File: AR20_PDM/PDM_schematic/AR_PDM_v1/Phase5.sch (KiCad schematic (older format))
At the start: 10 parts, among them Q3 BTS50025-1TAD, U4 INA233

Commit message: Working on pcb layout
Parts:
- removed D?: D_Schottky_x2, symbol AR20_PDM_v1-rescue:D_Schottky_x2
- added D45, D46: D_Schottky_BAT60A, AR_PDM_v1:D_Shotky_BAT60_HandSoldering, symbol AR20_PDM_v1-rescue:D_Schottky_BAT60A
- gave numbers to parts that had none: 4
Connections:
- net GND: now also D45.2 (A), D46.2 (A)
- net at R28.1, U4.10 (IN+): now also D46.1 (K)
- net at R24.1, U4.9 (In-): now also D45.1 (K)
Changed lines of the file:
@@
 AR Path="/5E0FBBBD/5EE9B23A" Ref="R?"  Part="1"
 AR Path="/5E0FC3A2/5EE9B23A" Ref="R?"  Part="1"
-AR Path="/5E0FCFDC/5EE9B23A" Ref="R?"  Part="1"
+AR Path="/5E0FCFDC/5EE9B23A" Ref="R25"  Part="1"
 AR Path="/5E0FDCCC/5EE9B23A" Ref="R?"  Part="1"
 AR Path="/5E10174B/5EE9B23A" Ref="R?"  Part="1"
-F 0 "R?" V 6643 1600 50  0000 C CNN
+F 0 "R25" V 6643 1600 50  0000 C CNN
 F 1 "2m_1%_4W" V 6734 1600 50  0000 C CNN
 F 2 "Resistor_SMD:R_2512_6332Metric" V 6780 1600 50  0001 C CNN
@@
 Text HLabel 7300 1600 2    50   Input ~ 10
 V+12V
-$Comp
-L AR20_PDM_v1-rescue:D_Schottky_x2 D?
-U 1 1 5EE9B241
-P 6950 4825
-AR Path="/5DA89415/5EE9B241" Ref="D?"  Part="1"
-AR Path="/5E0FCFDC/5EE9B241" Ref="D?"  Part="1"
-F 0 "D?" H 6950 5041 50  0000 C CNN
-F 1 "D_Schottky_x2" H 6950 4950 50  0000 C CNN
-F 2 "" H 6950 4825 50  0001 C CNN
-F 3 "~" H 6950 4825 50  0001 C CNN
-	1    6950 4825
-	1    0    0    -1
-$EndComp
 $Comp
 L AR20_PDM_v1-rescue:R-Device R?
@@
 AR Path="/5E0FBBBD/5EE9B247" Ref="R?"  Part="1"
 AR Path="/5E0FC3A2/5EE9B247" Ref="R?"  Part="1"
-AR Path="/5E0FCFDC/5EE9B247" Ref="R?"  Part="1"
+AR Path="/5E0FCFDC/5EE9B247" Ref="R24"  Part="1"
 AR Path="/5E0FDCCC/5EE9B247" Ref="R?"  Part="1"
 AR Path="/5E10174B/5EE9B247" Ref="R?"  Part="1"
-F 0 "R?" V 6443 3850 50  0000 C CNN
+F 0 "R24" V 6443 3850 50  0000 C CNN
 F 1 "1K_1%" V 6534 3850 50  0000 C CNN
 F 2 "Resistor_SMD:R_0603_1608Metric" V 6580 3850 50  0001 C CNN
@@
 AR Path="/5E0FBBBD/5EE9B24D" Ref="R?"  Part="1"
 AR Path="/5E0FC3A2/5EE9B24D" Ref="R?"  Part="1"
-AR Path="/5E0FCFDC/5EE9B24D" Ref="R?"  Part="1"
+AR Path="/5E0FCFDC/5EE9B24D" Ref="R28"  Part="1"
 AR Path="/5E0FDCCC/5EE9B24D" Ref="R?"  Part="1"
 AR Path="/5E10174B/5EE9B24D" Ref="R?"  Part="1"
-F 0 "R?" V 6843 3850 50  0000 C CNN
+F 0 "R28" V 6843 3850 50  0000 C CNN
 F 1 "1K_1%" V 6934 3850 50  0000 C CNN
 F 2 "Resistor_SMD:R_0603_1608Metric" V 6980 3850 50  0001 C CNN
@@
 Text Notes 7075 2000 0    50   ~ 10
 Place shunt and INA233 close, \nroute togethere, differentialy pair. \nKeep short, and away from Noise.
-$Comp
-L AR20_PDM_v1-rescue:GND-power #PWR?
-U 1 1 5EE9B25B
-P 6950 5025
-AR Path="/5DA89415/5EE9B25B" Ref="#PWR?"  Part="1"
-AR Path="/5DEB10A1/5EE9B25B" Ref="#PWR?"  Part="1"
-AR Path="/5DEB20EA/5EE9B25B" Ref="#PWR?"  Part="1"
-AR Path="/5E0E4725/5EE9B25B" Ref="#PWR?"  Part="1"
-AR Path="/5E0E4A93/5EE9B25B" Ref="#PWR?"  Part="1"
-AR Path="/5E0E4EB5/5EE9B25B" Ref="#PWR?"  Part="1"
-AR Path="/5E0E5304/5EE9B25B" Ref="#PWR?"  Part="1"
-AR Path="/5E0E594B/5EE9B25B" Ref="#PWR?"  Part="1"
-AR Path="/5E0E607C/5EE9B25B" Ref="#PWR?"  Part="1"
-AR Path="/5E0FB5C8/5EE9B25B" Ref="#PWR?"  Part="1"
-AR Path="/5E0FBBBD/5EE9B25B" Ref="#PWR?"  Part="1"
-AR Path="/5E0FC3A2/5EE9B25B" Ref="#PWR?"  Part="1"
-AR Path="/5E0FCFDC/5EE9B25B" Ref="#PWR?"  Part="1"
-AR Path="/5E0FDCCC/5EE9B25B" Ref="#PWR?"  Part="1"
-AR Path="/5E10174B/5EE9B25B" Ref="#PWR?"  Part="1"
-F 0 "#PWR?" H 6950 4775 50  0001 C CNN
-F 1 "GND" H 6955 4852 50  0000 C CNN
-F 2 "" H 6950 5025 50  0001 C CNN
-F 3 "" H 6950 5025 50  0001 C CNN
-	1    6950 5025
-	1    0    0    -1
-$EndComp
 Wire Wire Line
 	4775 1600 6650 1600
@@
 Wire Wire Line
 	6650 4400 8750 4400
-Connection ~ 6650 4400
-Wire Wire Line
-	6650 4400 6650 4825
-Wire Wire Line
-	8750 4300 7250 4300
-Wire Wire Line
-	7250 4825 7250 4300
-Connection ~ 7250 4300
-Wire Wire Line
-	7250 4300 7050 4300
 $Comp
 L AR20_PDM_v1-rescue:R-Device R?
@@
 AR Path="/5E0FBBBD/5EEC5BEE" Ref="R?"  Part="1"
 AR Path="/5E0FC3A2/5EEC5BEE" Ref="R?"  Part="1"
-AR Path="/5E0FCFDC/5EEC5BEE" Ref="R?"  Part="1"
+AR Path="/5E0FCFDC/5EEC5BEE" Ref="R29"  Part="1"
 AR Path="/5E0FDCCC/5EEC5BEE" Ref="R?"  Part="1"
 AR Path="/5E10174B/5EEC5BEE" Ref="R?"  Part="1"
-F 0 "R?" V 8093 4100 50  0000 C CNN
+F 0 "R29" V 8093 4100 50  0000 C CNN
 F 1 "10K" V 8184 4100 50  0000 C CNN
 F 2 "Resistor_SMD:R_0603_1608Metric" V 8230 4100 50  0001 C CNN
@@
 Text HLabel 8150 4100 0    50   Output ~ 10
 P5_OUT
+Wire Wire Line
+	7050 4300 7100 4300
+$Comp
+L AR20_PDM_v1-rescue:D_Schottky_BAT60A D?
+U 1 1 5EFAD5C9
+P 6700 4775
+AR Path="/5DA89415/5EFAD5C9" Ref="D?"  Part="1"
+AR Path="/5E0FCFDC/5EFAD5C9" Ref="D45"  Part="1"
+F 0 "D45" V 6530 4885 50  0000 L CNN
+F 1 "D_Schottky_BAT60A" V 6621 4885 50  0000 L CNN
+F 2 "AR_PDM_v1:D_Shotky_BAT60_HandSoldering" H 6800 4725 50  0001 C CNN
+F 3 "~" H 6800 4725 50  0001 C CNN
+	1    6700 4775
+	0    1    1    0
+$EndComp
+$Comp
+L AR20_PDM_v1-rescue:GND-power #PWR?
+U 1 1 5EFAD5CF
+P 6875 4950
+AR Path="/5DA89415/5EFAD5CF" Ref="#PWR?"  Part="1"
+AR Path="/5DEB10A1/5EFAD5CF" Ref="#PWR?"  Part="1"
+AR Path="/5DEB20EA/5EFAD5CF" Ref="#PWR?"  Part="1"
+AR Path="/5E0E4725/5EFAD5CF" Ref="#PWR?"  Part="1"
+AR Path="/5E0E4A93/5EFAD5CF" Ref="#PWR?"  Part="1"
+AR Path="/5E0E4EB5/5EFAD5CF" Ref="#PWR?"  Part="1"
+AR Path="/5E0E5304/5EFAD5CF" Ref="#PWR?"  Part="1"
+AR Path="/5E0E594B/5EFAD5CF" Ref="#PWR?"  Part="1"
+AR Path="/5E0E607C/5EFAD5CF" Ref="#PWR?"  Part="1"
+AR Path="/5E0FB5C8/5EFAD5CF" Ref="#PWR?"  Part="1"
+AR Path="/5E0FBBBD/5EFAD5CF" Ref="#PWR?"  Part="1"
+AR Path="/5E0FC3A2/5EFAD5CF" Ref="#PWR?"  Part="1"
+AR Path="/5E0FCFDC/5EFAD5CF" Ref="#PWR05"  Part="1"
+AR Path="/5E0FDCCC/5EFAD5CF" Ref="#PWR?"  Part="1"
+AR Path="/5E10174B/5EFAD5CF" Ref="#PWR?"  Part="1"
+F 0 "#PWR05" H 6875 4700 50  0001 C CNN
+F 1 "GND" H 6880 4777 50  0000 C CNN
+F 2 "" H 6875 4950 50  0001 C CNN
+F 3 "" H 6875 4950 50  0001 C CNN
+	1    6875 4950
+	1    0    0    -1
+$EndComp
+$Comp
+L AR20_PDM_v1-rescue:D_Schottky_BAT60A D?
+U 1 1 5EFAD5D5
+P 7150 4775
+AR Path="/5DA89415/5EFAD5D5" Ref="D?"  Part="1"
+AR Path="/5E0FCFDC/5EFAD5D5" Ref="D46"  Part="1"
+F 0 "D46" V 6980 4885 50  0000 L CNN
+F 1 "D_Schottky_BAT60A" V 7071 4885 50  0000 L CNN
+F 2 "AR_PDM_v1:D_Shotky_BAT60_HandSoldering" H 7250 4725 50  0001 C CNN
+F 3 "~" H 7250 4725 50  0001 C CNN
+	1    7150 4775
+	0    1    1    0
+$EndComp
+Wire Wire Line
+	6650 4475 6650 4400
+Wire Wire Line
+	7100 4475 7100 4300
+Wire Wire Line
+	6650 4825 6875 4825
+Wire Wire Line
+	6875 4950 6875 4825
+Connection ~ 6875 4825
+Wire Wire Line
+	6875 4825 7100 4825
+Connection ~ 7100 4300
+Wire Wire Line
+	7100 4300 8750 4300
+Connection ~ 6650 4400
 $EndSCHEMATC

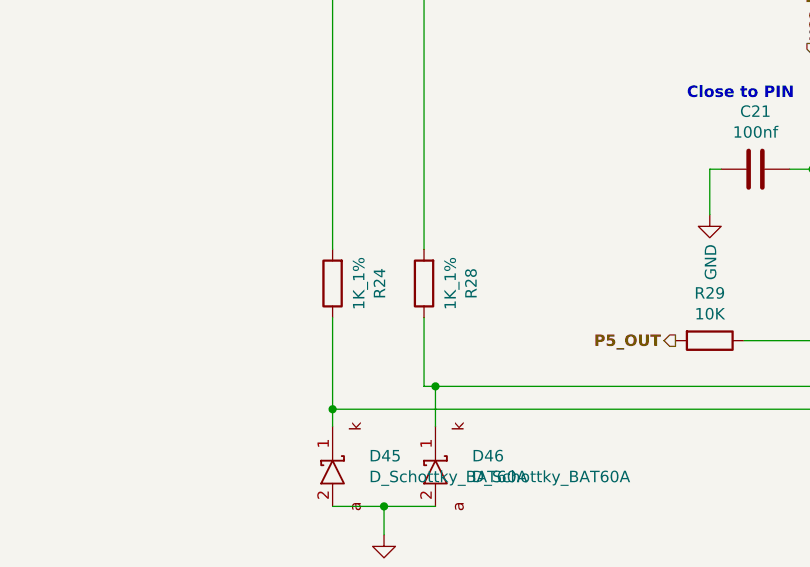
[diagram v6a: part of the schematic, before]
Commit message: shematics adjustments, and fixing values and names
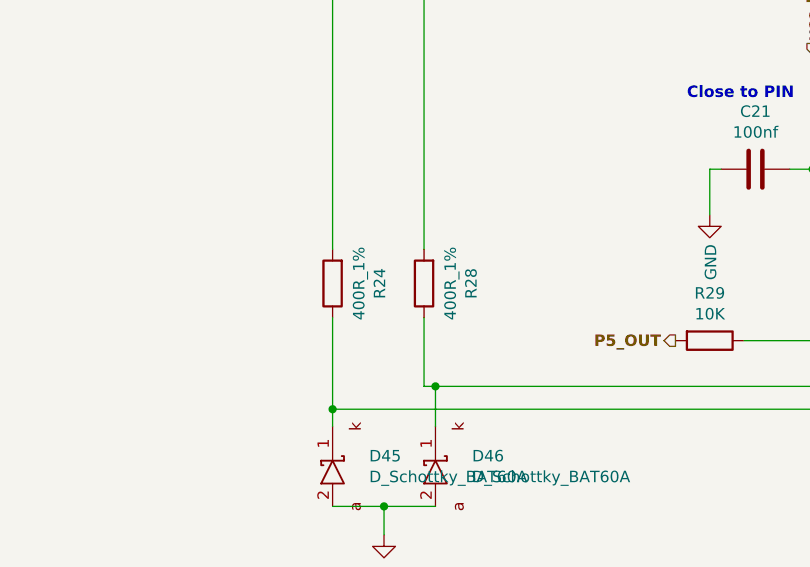
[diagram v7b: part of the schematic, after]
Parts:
- R24, R28: value 1K_1% -> 400R_1%
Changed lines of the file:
@@
 AR Path="/5E10174B/5EE9B247" Ref="R?"  Part="1"
 F 0 "R24" V 6443 3850 50  0000 C CNN
-F 1 "1K_1%" V 6534 3850 50  0000 C CNN
+F 1 "400R_1%" V 6534 3850 50  0000 C CNN
 F 2 "Resistor_SMD:R_0603_1608Metric" V 6580 3850 50  0001 C CNN
 F 3 "~" H 6650 3850 50  0001 C CNN
@@
 AR Path="/5E10174B/5EE9B24D" Ref="R?"  Part="1"
 F 0 "R28" V 6843 3850 50  0000 C CNN
-F 1 "1K_1%" V 6934 3850 50  0000 C CNN
+F 1 "400R_1%" V 6934 3850 50  0000 C CNN
 F 2 "Resistor_SMD:R_0603_1608Metric" V 6980 3850 50  0001 C CNN
 F 3 "~" H 7050 3850 50  0001 C CNN
